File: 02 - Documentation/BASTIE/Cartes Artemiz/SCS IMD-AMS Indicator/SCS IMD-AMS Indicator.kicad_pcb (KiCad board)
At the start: 2 copper layers, 33 x 33.3 mm, 21 parts, among them J1 2P Droit 2-11-2022, J2 2P Droit 2-11-2022, K1 SSR CPC1394GR, U2 Opamp_Dual, U3 Alim LP TSR_0.5-2450

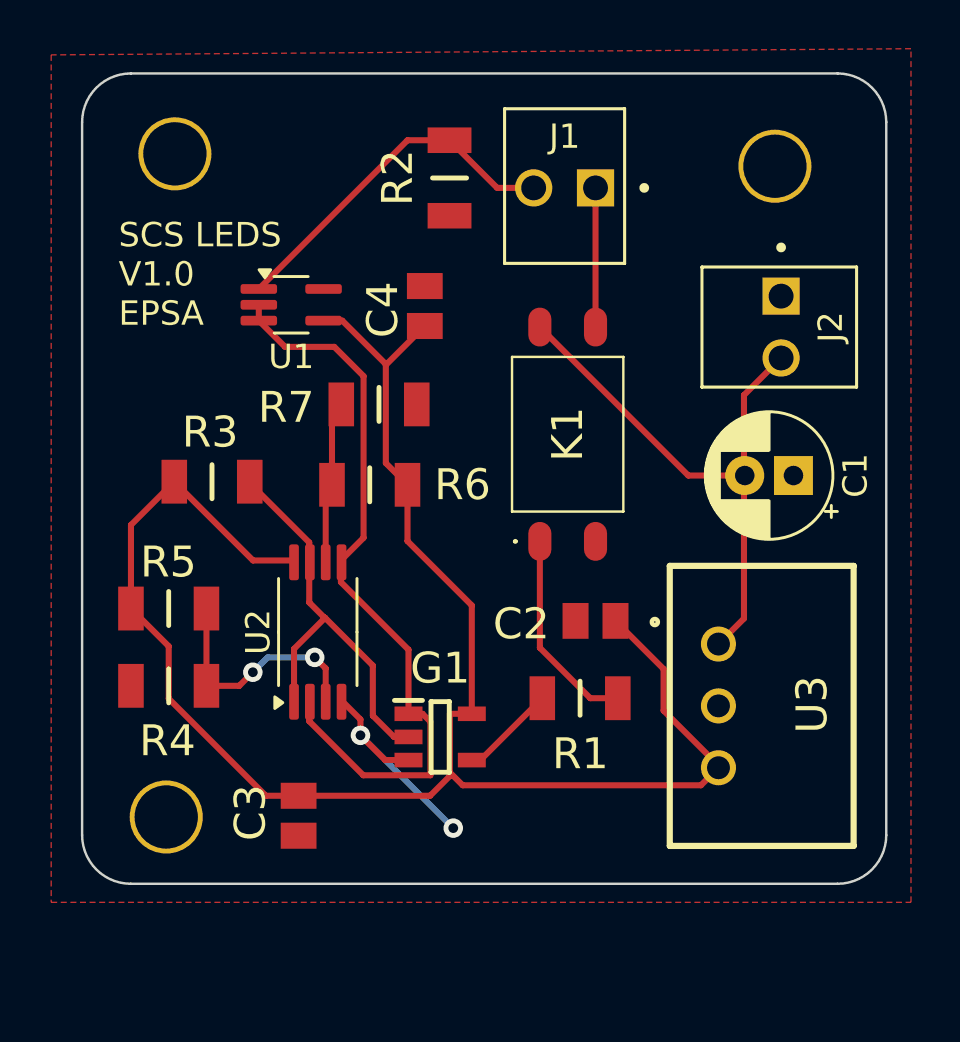
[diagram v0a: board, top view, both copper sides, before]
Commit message: PCBs + fichiers de fabrication
Update SCS LEDs et retours TSAL ESF
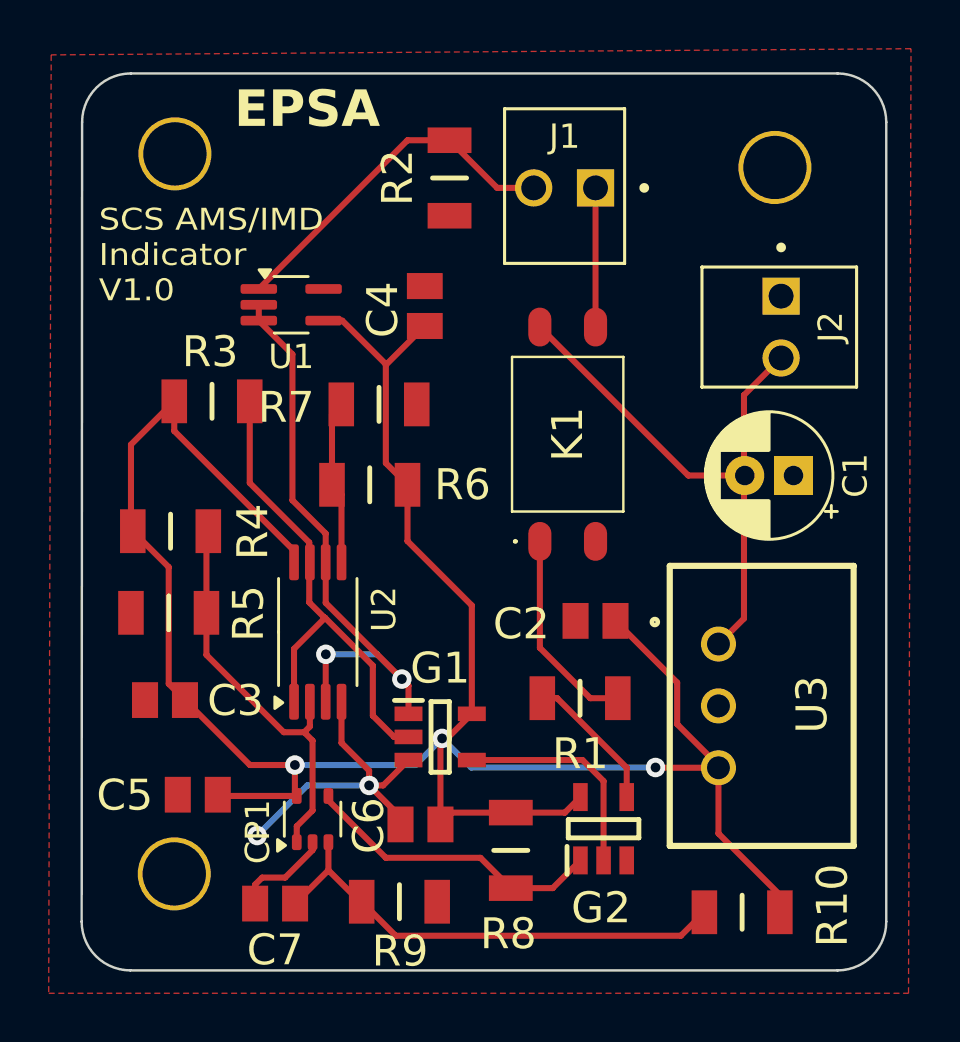
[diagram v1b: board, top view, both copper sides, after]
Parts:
- removed the ? at (96.3, 51.8)
- removed the ? at (71.3, 78.5)
- added ?: , , F.Cu at (96.3, 51.9)
- added ?: , , F.Cu at (71.6, 80.9)
- added C5: 10n, EPSA_lib:CAPC2012X130N, F.Cu at (72.6, 77.6)
- added C6: 10n, EPSA_lib:CAPC2012X130N, F.Cu at (81.7, 78.8)
- added C7: 22u, EPSA_lib:CAPC2012X130N, F.Cu at (75.7, 82.1)
- added CP1: Comparator, Package_TO_SOT_SMD:SOT-353_SC-70-5, F.Cu at (77.3, 78.6)
- added G2: Gate OR SN74AHCT1G32DBVR, EPSA_lib:SOT95P280X145-5N, F.Cu at (89.2, 79.0)
- added R10: 560k, EPSA_lib:RESC3216X70N, F.Cu at (94.9, 82.4)
- added R8: 10k, EPSA_lib:RESC3216X70N, F.Cu at (85.4, 79.9)
- added R9: 560k, EPSA_lib:RESC3216X70N, F.Cu at (80.8, 82.0)
- G1: value Gate OR SN74AHCT1G32DBVR -> Gate NAND SN74AHCT1G00DBVR
- moved C3 7.26 mm to (71.2, 73.7), turned to 0 degrees
- moved R3 3.30 mm to (73.2, 61.5)
- moved R4 3.18 mm to (71.5, 66.8)
- moved R5 3.00 mm to (71.4, 70.2)
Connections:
- net /Raw_LED_On renamed /Raw_PCB_State_OK
- net /SCS_Failure renamed /SCS_Compliance
- G1 pad 1: /LED_On -> /PCB_State_OK
- G1 pad 4: Net-(G1-Y) -> Net-(G1-Pad4)
- R1 pad 2: Net-(G1-Y) -> Net-(G2-Pad4)
- U1 pad 2: /LED_On -> /PCB_State_OK
- U1 pad 3: /LED_On -> /PCB_State_OK
- U2 pad 2: /LED_On -> /0.75V
- U2 pad 3: /0.75V -> /PCB_State_OK
- U2 pad 5: /LED_On -> /4.25V
- U2 pad 6: /4.25V -> /PCB_State_OK
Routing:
- net /LED_On: track 31.3 -> 0.00 mm
- net /PCB_State_OK: track 0.00 -> 24.8 mm, vias 0 -> 2
- net +5V: track 74.2 -> 98.4 mm, vias 0 -> 3
- net Net-(CP1--): track 0.00 -> 20.0 mm
- net /Visible_check: track 0.00 -> 12.5 mm
- net Net-(G1-Pad4): track 0.00 -> 9.02 mm
- net GND: track 9.57 -> 18.1 mm
- net /0.75V: track 10.1 -> 16.7 mm, vias 2 -> 0
- net Net-(G2-Pad4): track 0.00 -> 5.85 mm
- net Net-(G1-Y): track 3.95 -> 0.00 mm
- net /SCS_Compliance: track 17.5 -> 20.8 mm
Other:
- board size 33 x 33.3 mm -> 33 x 36.8 mm
- board text added: "EPSA"
- board text added: "SCS AMS/IMD Indicator V1.0"
- board text removed: "SCS LEDS V1.0 EPSA"

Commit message: Aop fixes
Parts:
- removed ? (x3): , 
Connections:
- U1 pad 2: /PCB_State_OK -> GND
- U1 pad 4: +5V -> /PCB_State_OK
- U1 pad 5: GND -> +5V
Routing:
- net /PCB_State_OK: track 24.8 -> 27.1 mm
- net GND: track 18.1 -> 20.0 mm
- net +5V: track 98.4 -> 99.9 mm
